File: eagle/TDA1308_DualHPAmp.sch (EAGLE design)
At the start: 28 parts, among them IC1 TDA1308, IC2 TDA1308

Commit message: Update
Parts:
- C2: value (none) -> 1uF
- R4: value 1uF -> 100k
- renumbered U$1 to POT1, U$2 to IC3, U$3 to JACK1, U$4 to JACK2, U$5 to JACK3
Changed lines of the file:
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@@
 <part name="SUPPLY3" library="supply2" deviceset="GND" device=""/>
 <part name="C1" library="rcl" deviceset="C-EU" device="050-050X075" value="1uF"/>
-<part name="C2" library="rcl" deviceset="C-EU" device="050-050X075"/>
+<part name="C2" library="rcl" deviceset="C-EU" device="050-050X075" value="1uF"/>
 <part name="R1" library="rcl" deviceset="R-EU_" device="0207/2V" value="100k"/>
-<part name="R4" library="rcl" deviceset="R-EU_" device="0207/2V" value="1uF"/>
+<part name="R4" library="rcl" deviceset="R-EU_" device="0207/2V" value="100k"/>
 <part name="SUPPLY4" library="supply2" deviceset="GND" device=""/>
 <part name="SUPPLY5" library="supply2" deviceset="GND" device=""/>
@@
 <part name="R11" library="rcl" deviceset="R-EU_" device="0207/7" value="6.8k"/>
 <part name="LED1" library="led" deviceset="LED" device="3MM" value="Blue"/>
-<part name="U$2" library="tle2426" deviceset="TLE2426*L" device="P" technology="C"/>
+<part name="IC3" library="tle2426" deviceset="TLE2426*L" device="P" technology="C"/>
 <part name="C3" library="rcl" deviceset="CPOL-EU" device="E2.5-7" value="100u"/>
 <part name="C4" library="rcl" deviceset="CPOL-EU" device="E2.5-7" value="100u"/>
@@
 <part name="SUPPLY16" library="supply2" deviceset="VCC" device=""/>
 <part name="FRAME1" library="frames" deviceset="A4L-LOC" device="" value="Schematic"/>
-<part name="U$1" library="mylib2" deviceset="RK0971221" device=""/>
-<part name="U$3" library="mylib2" deviceset="MJ-353W-0" device=""/>
-<part name="U$4" library="mylib2" deviceset="MJ-353W-0" device=""/>
-<part name="U$5" library="mylib2" deviceset="MJ-353W-0" device=""/>
+<part name="POT1" library="mylib2" deviceset="RK0971221" device=""/>
+<part name="JACK1" library="mylib2" deviceset="MJ-353W-0" device=""/>
+<part name="JACK2" library="mylib2" deviceset="MJ-353W-0" device=""/>
+<part name="JACK3" library="mylib2" deviceset="MJ-353W-0" device=""/>
 <part name="SUPPLY17" library="supply2" deviceset="GND" device=""/>
 </parts>
@@
 <instance part="R11" gate="G$1" x="187.96" y="152.4" rot="R90"/>
 <instance part="LED1" gate="G$1" x="187.96" y="142.24"/>
-<instance part="U$2" gate="G$1" x="203.2" y="147.32"/>
+<instance part="IC3" gate="G$1" x="203.2" y="147.32"/>
 <instance part="C3" gate="G$1" x="218.44" y="142.24"/>
 <instance part="C4" gate="G$1" x="218.44" y="154.94"/>
@@
 <instance part="SUPPLY16" gate="G$1" x="238.76" y="162.56"/>
 <instance part="FRAME1" gate="G$1" x="0" y="0"/>
-<instance part="U$1" gate="G$1" x="50.8" y="154.94"/>
-<instance part="U$1" gate="G$2" x="50.8" y="116.84"/>
-<instance part="U$1" gate="G$3" x="172.72" y="157.48" rot="MR270"/>
-<instance part="U$3" gate="G$1" x="17.78" y="157.48" rot="MR0"/>
-<instance part="U$4" gate="G$1" x="134.62" y="147.32"/>
-<instance part="U$5" gate="G$1" x="134.62" y="68.58"/>
+<instance part="POT1" gate="G$1" x="50.8" y="154.94"/>
+<instance part="POT1" gate="G$2" x="50.8" y="116.84"/>
+<instance part="POT1" gate="G$3" x="172.72" y="157.48" rot="MR270"/>
+<instance part="JACK1" gate="G$1" x="17.78" y="157.48" rot="MR0"/>
+<instance part="JACK2" gate="G$1" x="134.62" y="147.32"/>
+<instance part="JACK3" gate="G$1" x="134.62" y="68.58"/>
 <instance part="SUPPLY17" gate="GND" x="246.38" y="142.24"/>
 </instances>
@@
 <wire x1="25.4" y1="162.56" x2="50.8" y2="162.56" width="0.1524" layer="91"/>
 <wire x1="50.8" y1="162.56" x2="50.8" y2="160.02" width="0.1524" layer="91"/>
-<pinref part="U$1" gate="G$1" pin="E"/>
-<pinref part="U$3" gate="G$1" pin="2"/>
+<pinref part="POT1" gate="G$1" pin="E"/>
+<pinref part="JACK1" gate="G$1" pin="2"/>
 </segment>
 </net>
@@
 <wire x1="38.1" y1="137.16" x2="50.8" y2="137.16" width="0.1524" layer="91"/>
 <wire x1="50.8" y1="137.16" x2="50.8" y2="121.92" width="0.1524" layer="91"/>
-<pinref part="U$1" gate="G$2" pin="E"/>
-<pinref part="U$3" gate="G$1" pin="3"/>
+<pinref part="POT1" gate="G$2" pin="E"/>
+<pinref part="JACK1" gate="G$1" pin="3"/>
 </segment>
 </net>
@@
 <pinref part="SUPPLY2" gate="GND" pin="GND"/>
 <wire x1="50.8" y1="109.22" x2="50.8" y2="111.76" width="0.1524" layer="91"/>
-<pinref part="U$1" gate="G$2" pin="A"/>
+<pinref part="POT1" gate="G$2" pin="A"/>
 </segment>
 <segment>
 <pinref part="SUPPLY1" gate="GND" pin="GND"/>
 <wire x1="50.8" y1="147.32" x2="50.8" y2="149.86" width="0.1524" layer="91"/>
-<pinref part="U$1" gate="G$1" pin="A"/>
+<pinref part="POT1" gate="G$1" pin="A"/>
 </segment>
 <segment>
@@
 <wire x1="25.4" y1="152.4" x2="27.94" y2="152.4" width="0.1524" layer="91"/>
 <wire x1="27.94" y1="152.4" x2="27.94" y2="147.32" width="0.1524" layer="91"/>
-<pinref part="U$3" gate="G$1" pin="1"/>
+<pinref part="JACK1" gate="G$1" pin="1"/>
 </segment>
 <segment>
@@
 <wire x1="124.46" y1="139.7" x2="124.46" y2="142.24" width="0.1524" layer="91"/>
 <wire x1="124.46" y1="142.24" x2="127" y2="142.24" width="0.1524" layer="91"/>
-<pinref part="U$4" gate="G$1" pin="1"/>
+<pinref part="JACK2" gate="G$1" pin="1"/>
 </segment>
 <segment>
@@
 <wire x1="124.46" y1="60.96" x2="124.46" y2="63.5" width="0.1524" layer="91"/>
 <wire x1="124.46" y1="63.5" x2="127" y2="63.5" width="0.1524" layer="91"/>
-<pinref part="U$5" gate="G$1" pin="1"/>
+<pinref part="JACK3" gate="G$1" pin="1"/>
 </segment>
 <segment>
@@
 <pinref part="C3" gate="G$1" pin="+"/>
 <wire x1="218.44" y1="149.86" x2="218.44" y2="147.32" width="0.1524" layer="91"/>
-<pinref part="U$2" gate="G$1" pin="OUT"/>
+<pinref part="IC3" gate="G$1" pin="OUT"/>
 <wire x1="218.44" y1="147.32" x2="218.44" y2="144.78" width="0.1524" layer="91"/>
 <wire x1="210.82" y1="147.32" x2="218.44" y2="147.32" width="0.1524" layer="91"/>
@@
 <pinref part="C1" gate="G$1" pin="1"/>
 <wire x1="55.88" y1="154.94" x2="58.42" y2="154.94" width="0.1524" layer="91"/>
-<pinref part="U$1" gate="G$1" pin="S"/>
+<pinref part="POT1" gate="G$1" pin="S"/>
 </segment>
 </net>
@@
 <pinref part="C2" gate="G$1" pin="1"/>
 <wire x1="55.88" y1="116.84" x2="58.42" y2="116.84" width="0.1524" layer="91"/>
-<pinref part="U$1" gate="G$2" pin="S"/>
+<pinref part="POT1" gate="G$2" pin="S"/>
 </segment>
 </net>
@@
 <wire x1="111.76" y1="152.4" x2="127" y2="152.4" width="0.1524" layer="91"/>
 <junction x="111.76" y="152.4"/>
-<pinref part="U$4" gate="G$1" pin="2"/>
+<pinref part="JACK2" gate="G$1" pin="2"/>
 </segment>
 </net>
@@
 <wire x1="218.44" y1="137.16" x2="218.44" y2="134.62" width="0.1524" layer="91"/>
 <junction x="218.44" y="134.62"/>
-<pinref part="U$2" gate="G$1" pin="COM"/>
+<pinref part="IC3" gate="G$1" pin="COM"/>
 <wire x1="200.66" y1="139.7" x2="200.66" y2="134.62" width="0.1524" layer="91"/>
 <junction x="200.66" y="134.62"/>
@@
 <pinref part="R11" gate="G$1" pin="2"/>
 <wire x1="187.96" y1="160.02" x2="187.96" y2="157.48" width="0.1524" layer="91"/>
-<pinref part="U$2" gate="G$1" pin="IN"/>
+<pinref part="IC3" gate="G$1" pin="IN"/>
 <wire x1="187.96" y1="160.02" x2="200.66" y2="160.02" width="0.1524" layer="91"/>
 <wire x1="200.66" y1="160.02" x2="200.66" y2="154.94" width="0.1524" layer="91"/>
@@
 <pinref part="SUPPLY16" gate="G$1" pin="VCC"/>
 <junction x="238.76" y="160.02"/>
-<pinref part="U$1" gate="G$3" pin="P"/>
+<pinref part="POT1" gate="G$3" pin="P"/>
 <wire x1="180.34" y1="160.02" x2="187.96" y2="160.02" width="0.1524" layer="91"/>
 <junction x="187.96" y="160.02"/>
@@
 <wire x1="116.84" y1="114.3" x2="111.76" y2="114.3" width="0.1524" layer="91"/>
 <junction x="111.76" y="114.3"/>
-<pinref part="U$4" gate="G$1" pin="3"/>
+<pinref part="JACK2" gate="G$1" pin="3"/>
 </segment>
 </net>
@@
 <wire x1="111.76" y1="73.66" x2="127" y2="73.66" width="0.1524" layer="91"/>
 <junction x="111.76" y="73.66"/>
-<pinref part="U$5" gate="G$1" pin="2"/>
+<pinref part="JACK3" gate="G$1" pin="2"/>
 </segment>
 </net>
@@
 <wire x1="116.84" y1="35.56" x2="111.76" y2="35.56" width="0.1524" layer="91"/>
 <junction x="111.76" y="35.56"/>
-<pinref part="U$5" gate="G$1" pin="3"/>
+<pinref part="JACK3" gate="G$1" pin="3"/>
 </segment>
 </net>
@@
 <wire x1="165.1" y1="157.48" x2="165.1" y2="162.56" width="0.1524" layer="91"/>
 <wire x1="165.1" y1="162.56" x2="170.18" y2="162.56" width="0.1524" layer="91"/>
-<pinref part="U$1" gate="G$3" pin="O"/>
-</segment>
-</net>
+<pinref part="POT1" gate="G$3" pin="O"/>
+</segment>
+</net>

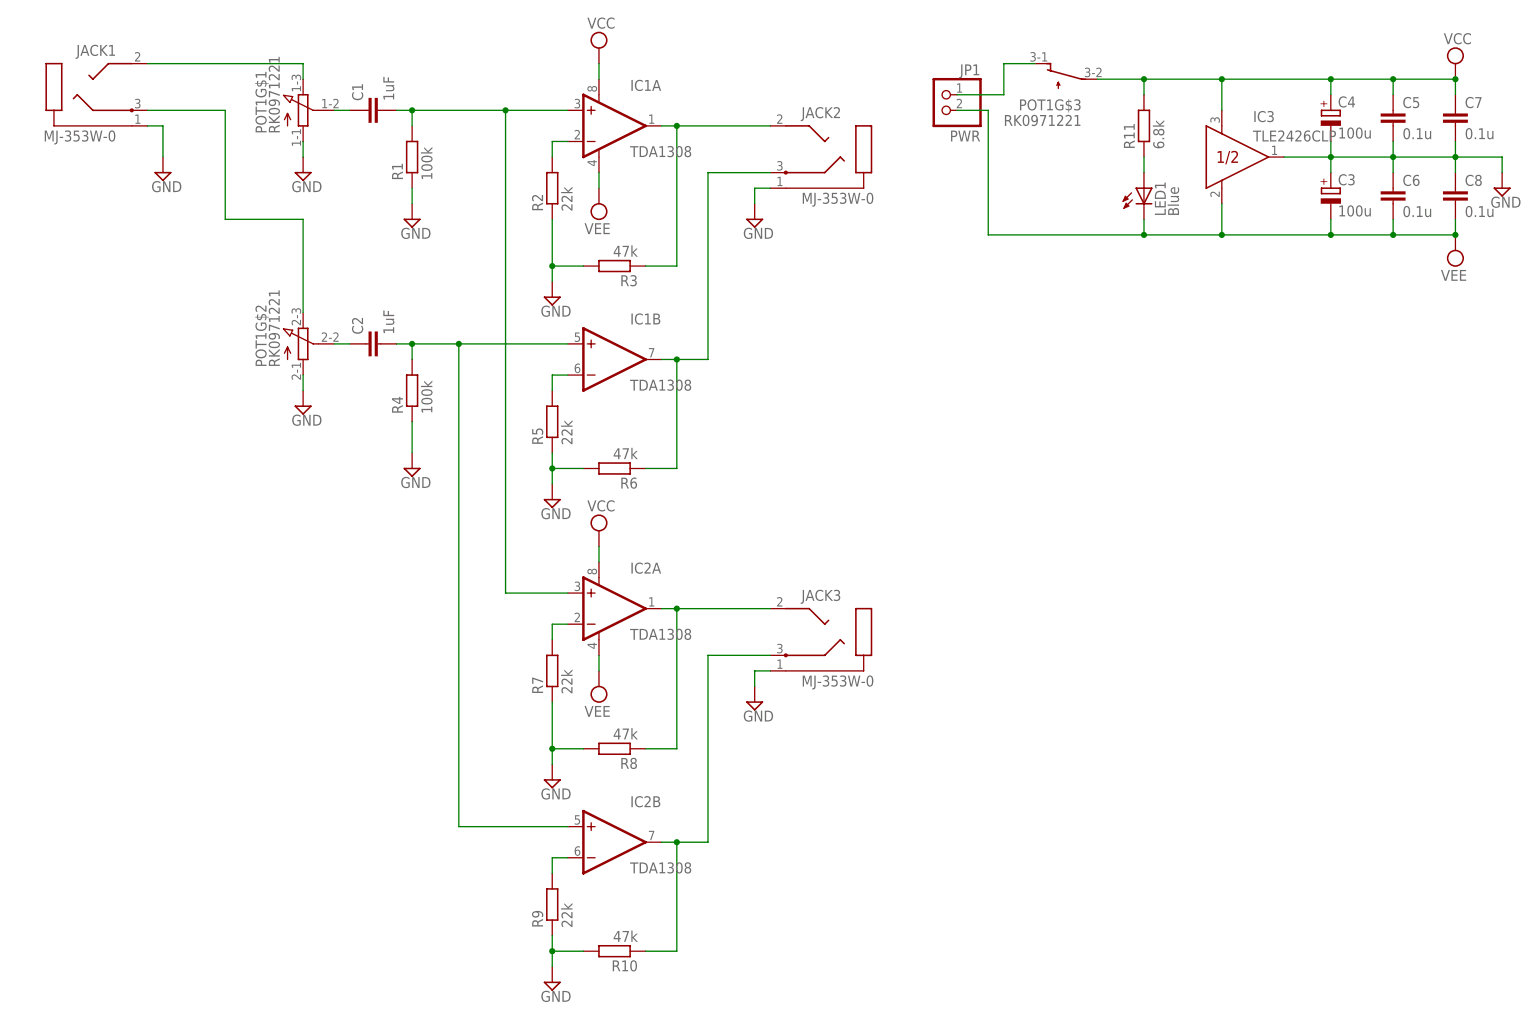
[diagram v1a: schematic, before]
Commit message: 非反転増幅回路のRの位置を修正
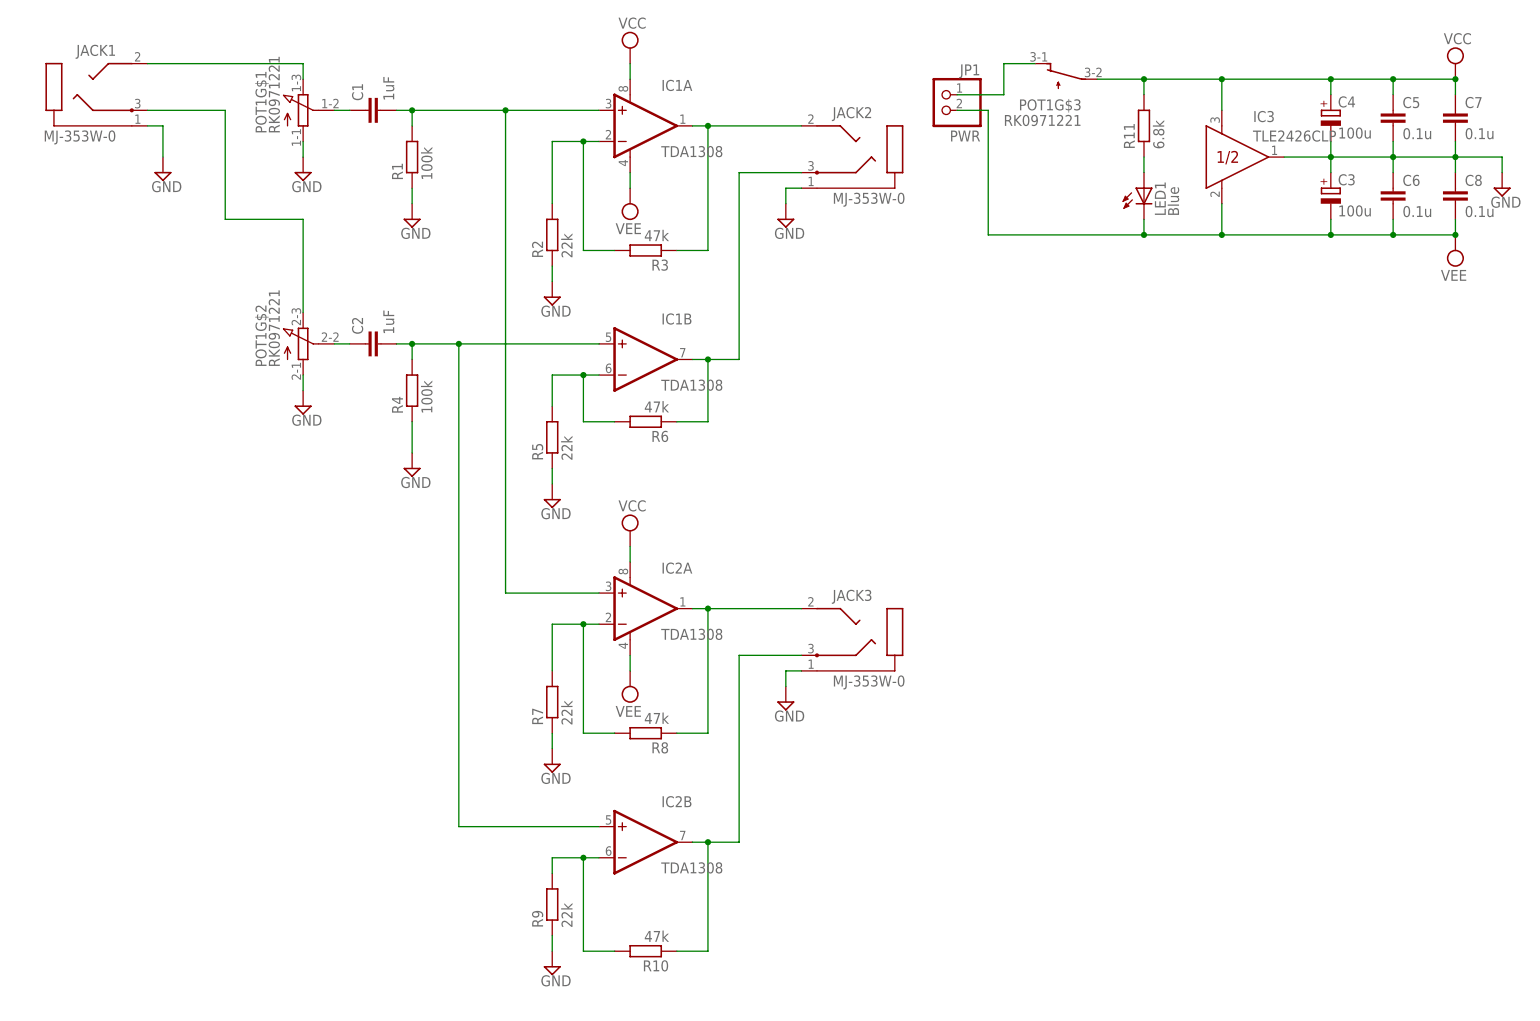
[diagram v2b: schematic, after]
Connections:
- removed net N$15: IC2A.-IN, R7.2
- removed net N$17: IC2B.-IN, R9.2
- new net N$12: IC2A.-IN, R7.2, R8.2
- new net N$14: IC2B.-IN, R10.2, R9.2
- net GND: no longer R10.2, R3.2, R6.2, R8.2
- net N$7: now also R3.2
- net N$9: now also R6.2
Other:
- moved on the sheet: IC1A, IC1B, IC2A, IC2B, JACK2, JACK3, R10, R2, R3, R5, R6, R7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
